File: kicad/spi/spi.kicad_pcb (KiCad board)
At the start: 2 copper layers, 102.5 x 44.8 mm, 18 parts, among them J1 Board Connector, J2 SPI 1, J3 IO Select, J4 SPI 2, J5 SPI 3, U1 TinyFPGA w/SPI Module, U2 TSR1-2433E, U3 SN74LVC8T245PWR, U4 SN74LVC8T245PWR, U5 FM25V05-G

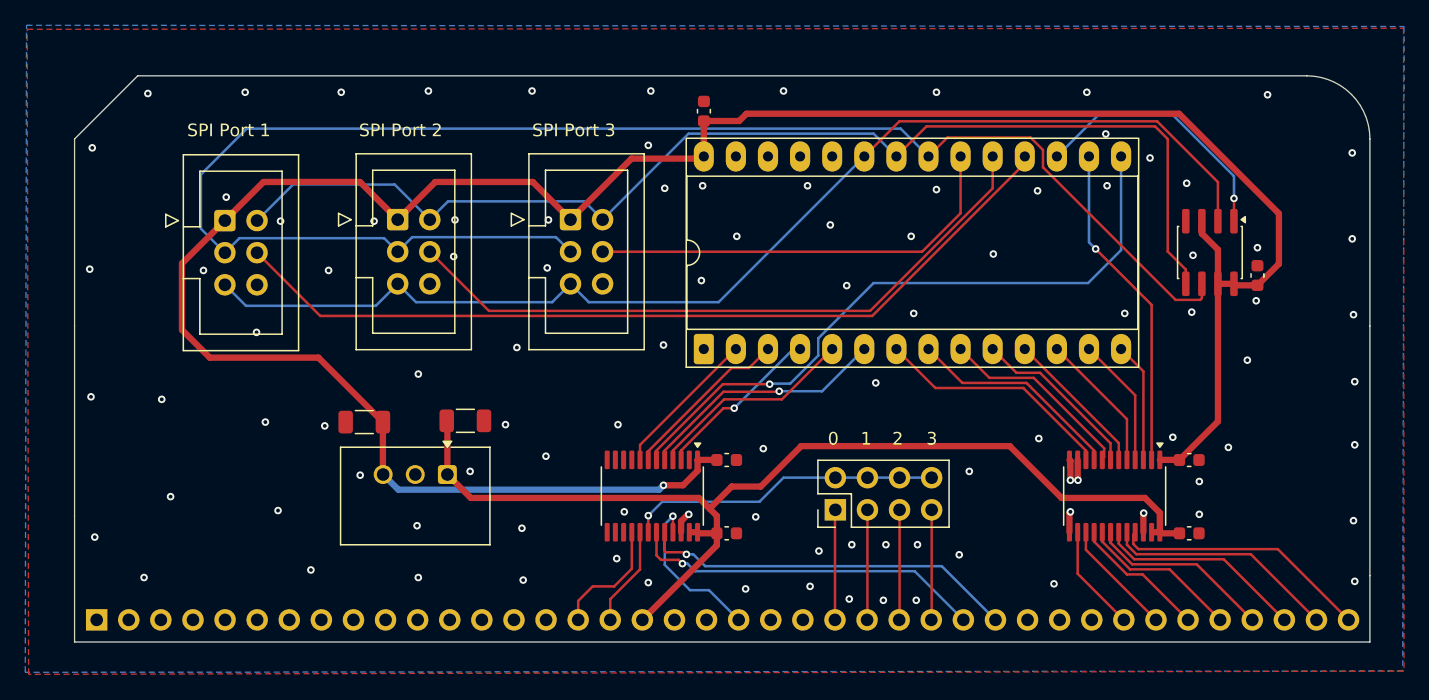
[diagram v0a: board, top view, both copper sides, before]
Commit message: setup eventual console output
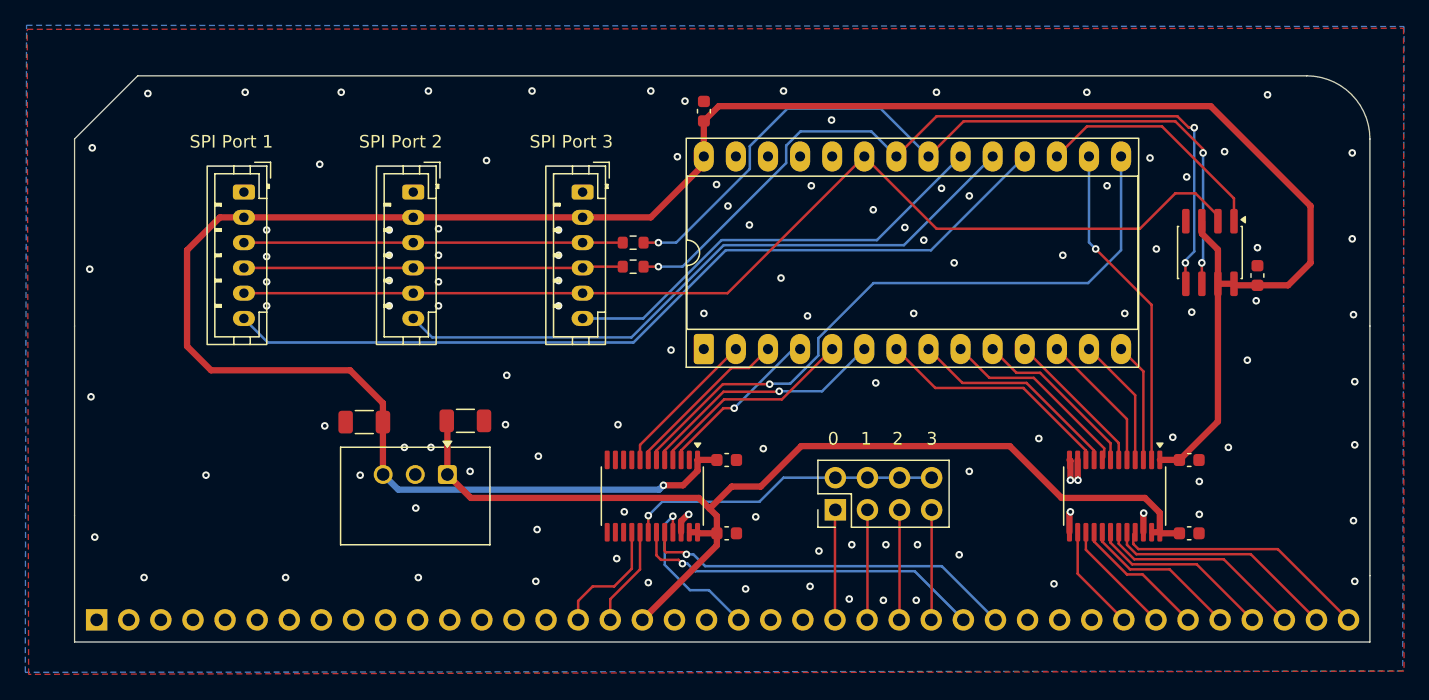
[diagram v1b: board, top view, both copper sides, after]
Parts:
- removed J2: SPI 1, Connector_IDC:IDC-Header_2x03_P2.54mm_Vertical
- removed J4: SPI 2, Connector_IDC:IDC-Header_2x03_P2.54mm_Vertical
- removed J5: SPI 3, Connector_IDC:IDC-Header_2x03_P2.54mm_Vertical
- added J6: SPI 1, Connector_JST:JST_PH_B6B-PH-K_1x06_P2.00mm_Vertical, F.Cu at (83.4, 94.4)
- added J7: SPI 2, Connector_JST:JST_PH_B6B-PH-K_1x06_P2.00mm_Vertical, F.Cu at (96.8, 94.4)
- added J8: SPI 3, Connector_JST:JST_PH_B6B-PH-K_1x06_P2.00mm_Vertical, F.Cu at (110.2, 94.4)
- added R1: 33, Resistor_SMD:R_0603_1608Metric, F.Cu at (114.2, 98.4)
- added R2: 33, Resistor_SMD:R_0603_1608Metric, F.Cu at (114.2, 100.3)
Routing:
- net SCK: track 125.8 -> 64.0 mm, vias 0 -> 3
- net MOSI_OUT: track 0.00 -> 30.0 mm
- net SCK_OUT: track 0.00 -> 30.0 mm
- net MOSI: track 92.6 -> 64.0 mm, vias 0 -> 3
- net MISO: track 92.8 -> 86.3 mm
- net 3v3: track 190.4 -> 193.3 mm
- net SPI_CSB0: track 21.1 -> 19.2 mm, vias 1 -> 0
- net SPI_CSB3: track 34.1 -> 35.2 mm
- net SPI_CSB1: track 68.4 -> 69.2 mm
- net SPI_CSB2: track 53.0 -> 52.4 mm
- net GND: vias 101 -> 112

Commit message: added spi and via boards
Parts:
- J6, J7, J8: footprint Connector_JST:JST_PH_B6B-PH-K_1x06_P2.00mm_Vertical -> Connector_JST:JST_XH_B6B-XH-AM_1x06_P2.50mm_Vertical
- moved J8 4.25 mm to (106.5, 92.3)
- moved J7 3.66 mm to (93.8, 92.3)
- moved J6 3.11 mm to (81.1, 92.3)
- moved R1 1.12 mm to (114.0, 97.3)
- moved R2 0.54 mm to (114.0, 99.8)
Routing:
- net 3v3: track 193.3 -> 202.2 mm
- net SPI_CSB3: track 35.2 -> 39.1 mm
- net SPI_CSB2: track 52.4 -> 55.9 mm
- net SPI_CSB1: track 69.2 -> 72.0 mm
- net MISO: track 86.3 -> 88.5 mm
- net SCK_OUT: track 30.0 -> 32.1 mm
- net MOSI_OUT: track 30.0 -> 32.1 mm
- net 5V: track 83.1 -> 84.8 mm
- net GND: vias 112 -> 119
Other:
- board text added: "IO Select"
